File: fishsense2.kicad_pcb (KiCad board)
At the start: 4 copper layers, 97.8 x 109.9 mm, 41 parts, among them J1 Conn_02x10_Odd_Even, J10 USB_B_Micro, J11 Screw_Terminal_01x02, J2 BATT_OUT, J3 BATT_IN, J4 Barrel_Jack_Switch, J5 USB3_A, J6 USB3_A, J7 USB3_A, J8 USB3_A, J9 Barrel_Jack, K1 UMS05-1A80-75L, Q1 Q_NMOS_DGS, Q2 Q_NMOS_DSG, SW1 SW_Reed, SW2 SW_Reed, U5 P783F-Q24-S5-S

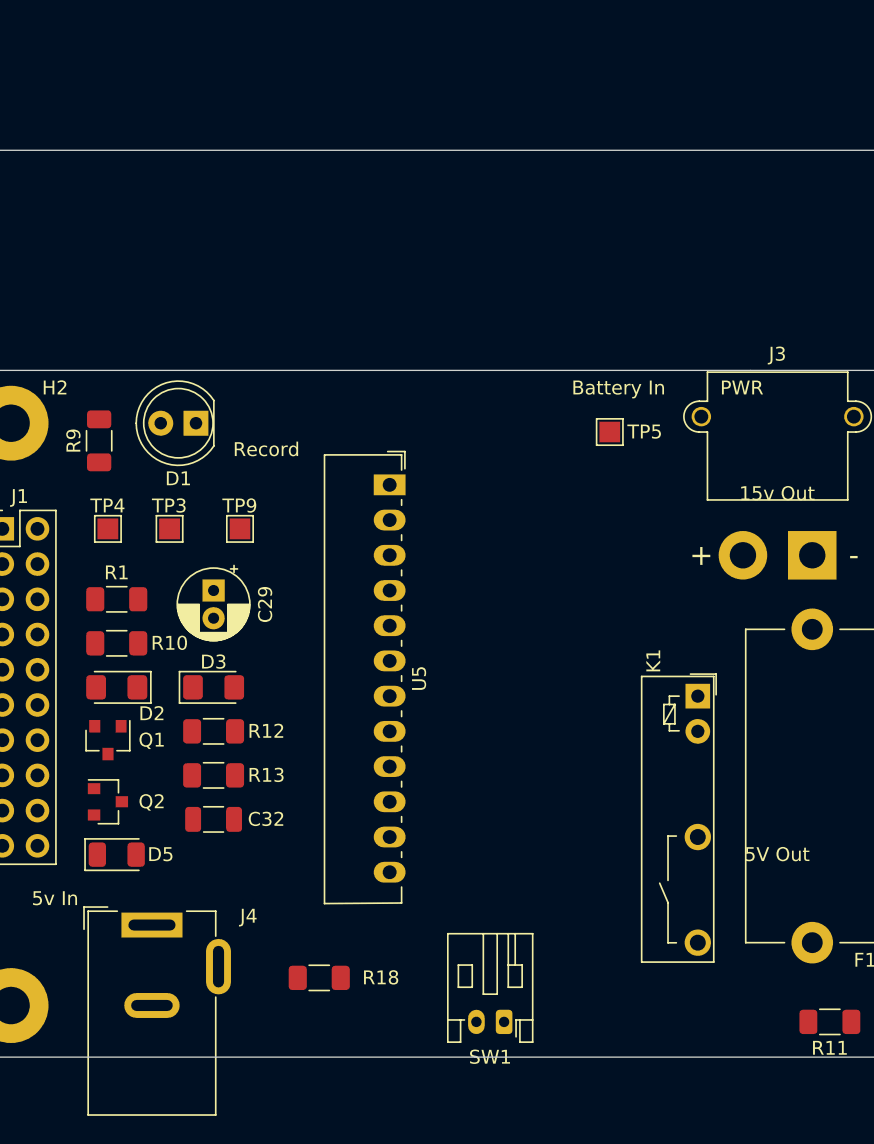
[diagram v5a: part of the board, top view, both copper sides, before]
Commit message: Removed uneeded DC barrel power. Adjusted component values for 12v supply. Checked footprints.
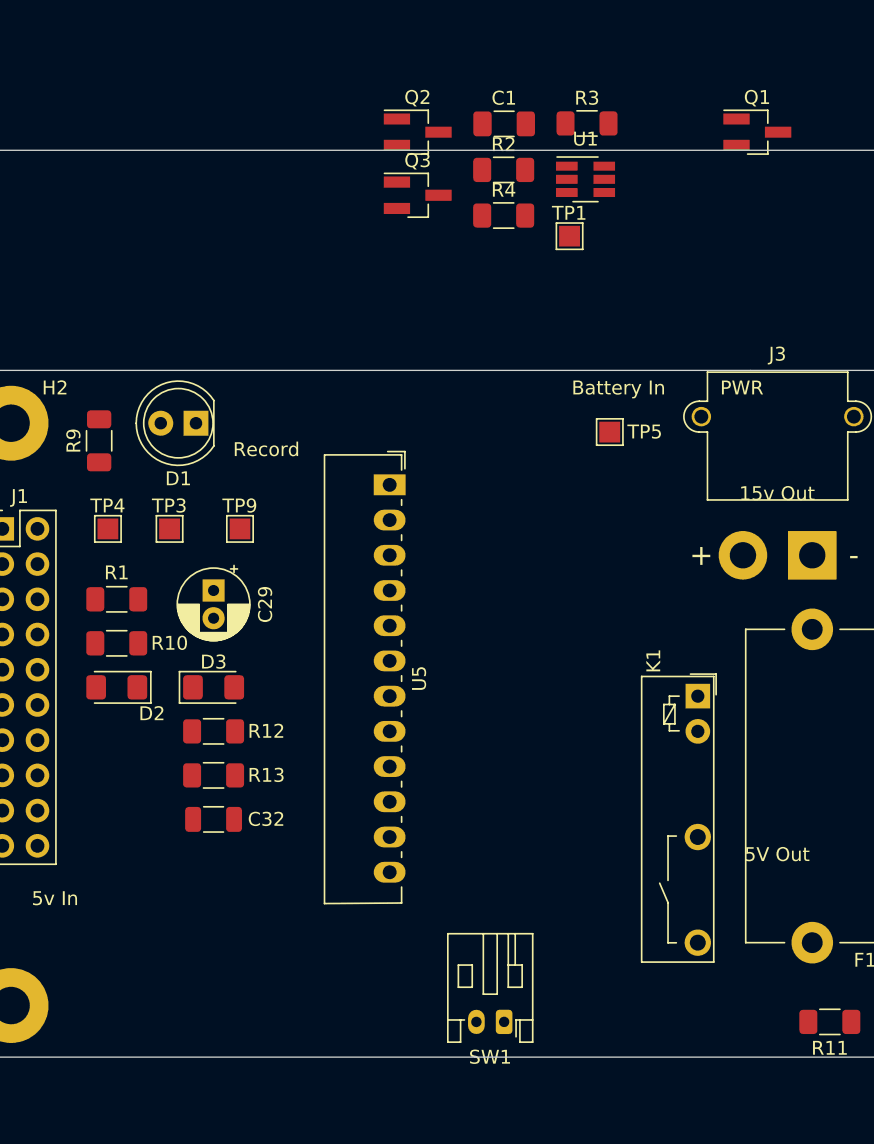
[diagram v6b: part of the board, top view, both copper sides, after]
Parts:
- removed D5: D_Schottky, Diode_SMD:D_1206_3216Metric
- removed J4: Barrel_Jack_Switch, Connector_BarrelJack:BarrelJack_Wuerth_6941xx301002
- removed R18: 125k, Resistor_SMD:R_1206_3216Metric_Pad1.30x1.75mm_HandSolder
- added C1: 10n, Capacitor_SMD:C_1206_3216Metric_Pad1.33x1.80mm_HandSolder, F.Cu at (156.2, 94.0)
- added Q3: Q_NMOS_GSD, Package_TO_SOT_SMD:SOT-23_Handsoldering, F.Cu at (150.0, 99.1)
- added R2: 100k, Resistor_SMD:R_1206_3216Metric_Pad1.30x1.75mm_HandSolder, F.Cu at (156.2, 97.3)
- added R3: 1M69, Resistor_SMD:R_1206_3216Metric_Pad1.30x1.75mm_HandSolder, F.Cu at (162.2, 94.0)
- added R4: 80k, Resistor_SMD:R_1206_3216Metric_Pad1.30x1.75mm_HandSolder, F.Cu at (156.2, 100.6)
- added TP1: Poweroff_OD, TestPoint:TestPoint_Pad_1.5x1.5mm, F.Cu at (160.9, 102.1)
- added U1: TPS3711, Package_TO_SOT_SMD:SOT-23-6_Handsoldering, F.Cu at (162.1, 98.0)
- Q1: value Q_NMOS_DGS -> Q_NMOS_GSD; footprint Package_TO_SOT_SMD:SOT-23 -> Package_TO_SOT_SMD:SOT-23_Handsoldering
- Q2: value Q_NMOS_DSG -> Q_NMOS_GSD; footprint Package_TO_SOT_SMD:SOT-23 -> Package_TO_SOT_SMD:SOT-23_Handsoldering
- R1: value 39k -> 30k
- R11: value 5k6 -> 300
- R12: value 20k -> 100k
- R13: value 40k -> 200k
- moved Q1 64.2 mm to (174.5, 94.6), turned to 0 degrees
- moved Q2 53.2 mm to (150.0, 94.6)
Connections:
- C32 pad 1: Net-(C32-Pad1) -> +5V
- F1 pad 1: +15V -> +12V
- J1 pad 8: REED -> Net-(J1-Pad8)
- J1 pad 9: Net-(J1-Pad9) -> REED
- K1 pad 4: +15V -> +12V
- Q1 pad 1: Net-(D1-Pad1) -> Net-(J1-Pad7)
- Q1 pad 2: Net-(J1-Pad7) -> GND
- Q1 pad 3: GND -> Net-(D1-Pad1)
- Q2 pad 1: /Power/RELAY- -> RELAY_CTL
- Q2 pad 2: /Power/BARREL_OPEN -> Net-(Q2-Pad2)
- Q2 pad 3: RELAY_CTL -> /Power/RELAY-
- R11 pad 1: +15V -> +12V
- R12 pad 1: +5V -> +12V
- SW1 pad 2: Net-(J1-Pad9) -> Net-(J1-Pad8)
- U5 pad 10: Net-(C32-Pad1) -> +5V
- U5 pad 11: Net-(C32-Pad1) -> +5V
- U5 pad 9: Net-(C32-Pad1) -> +5V

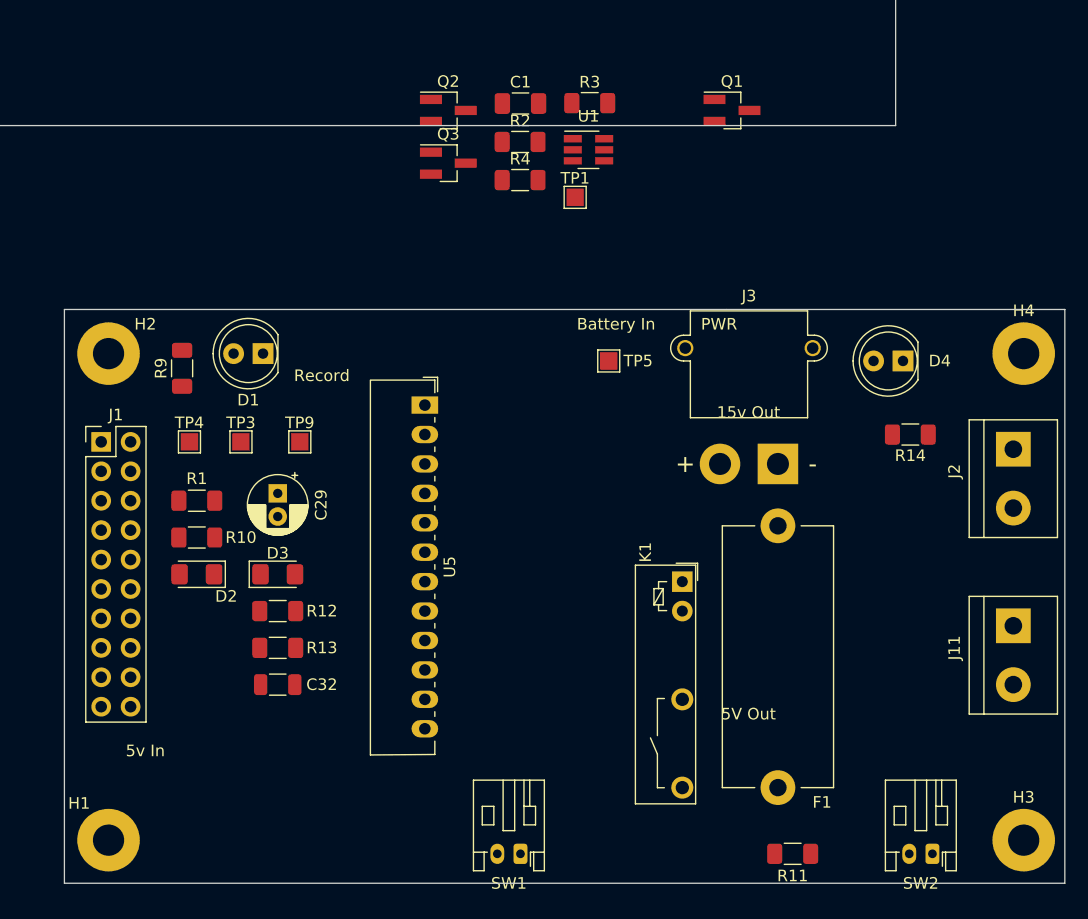
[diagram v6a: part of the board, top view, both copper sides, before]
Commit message: Moved components around on PCB. Fixed fuse footprint.
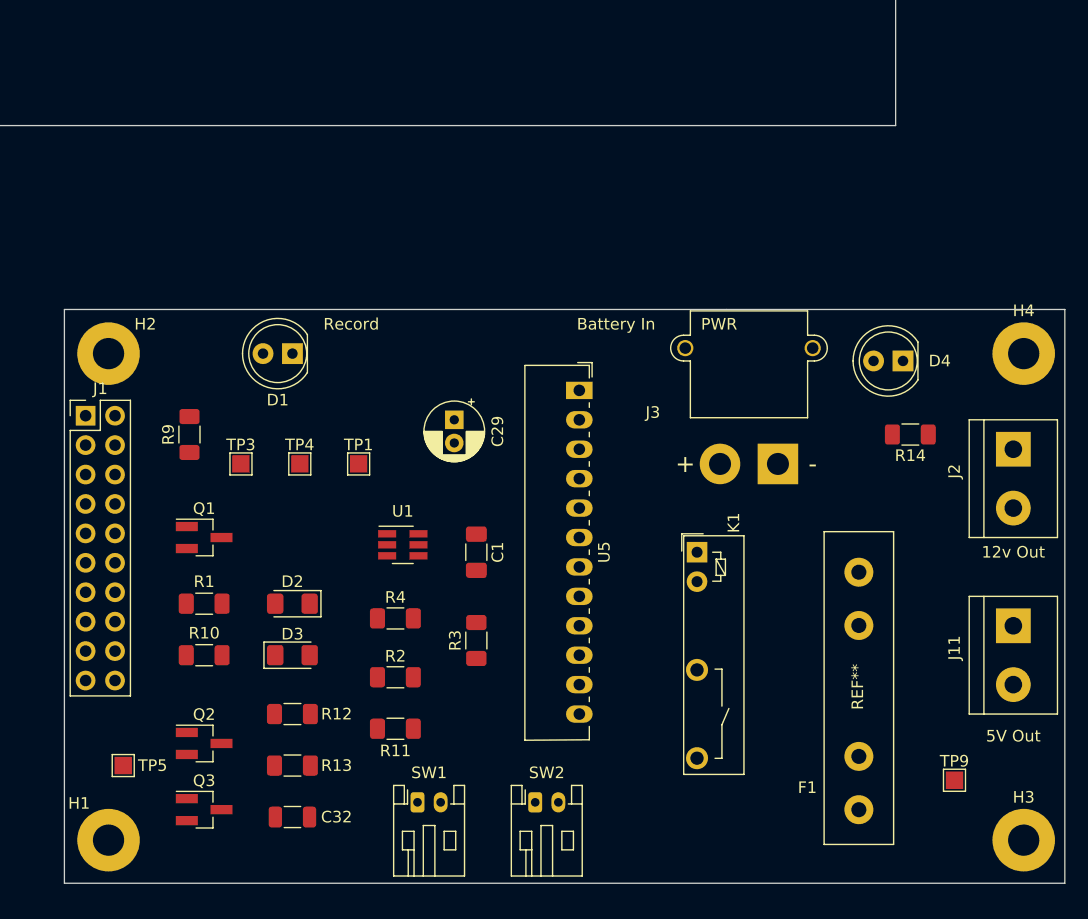
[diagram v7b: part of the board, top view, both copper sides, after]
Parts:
- F1: footprint Fuse:Fuseholder_Cylinder-5x20mm_Stelvio-Kontek_PTF78_Horizontal_Open -> fishsense2:5mm_Fuse_Clips
- moved TP9 63.6 mm to (193.7, 152.4)
- moved Q3 59.7 mm to (128.9, 154.9)
- moved Q1 58.6 mm to (128.9, 131.4)
- moved Q2 58.6 mm to (128.9, 149.2)
- moved TP5 54.6 mm to (121.9, 151.1)
- moved R2 47.4 mm to (145.4, 143.5)
- moved R3 47.4 mm to (152.4, 140.3), turned to 90 degrees
- moved R4 39.3 mm to (145.4, 138.4)
- moved C1 38.9 mm to (152.4, 132.7), turned to 270 degrees
- moved U1 37.7 mm to (146.1, 132.1)
- moved R11 35.9 mm to (145.4, 148.0)
- moved SW2 34.6 mm to (157.5, 154.3), turned to 0 degrees
- moved TP1 29.6 mm to (142.2, 125.1)
- moved C29 16.5 mm to (150.5, 121.3)
- moved U5 13.4 mm to (161.3, 118.7)
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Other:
- board text added: "12v Out"
- board text removed: "15v Out"
- board text removed: "5v In"

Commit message: Routed traces.
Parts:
- removed J10: USB_B_Micro, Connector_USB:USB_Micro-B_GCT_USB3076-30-A
- removed J5, J6, J7, J8: USB3_A, Connector_USB:USB3_A_Molex_48393-001
- removed J9: Barrel_Jack, Connector_BarrelJack:BarrelJack_Horizontal
- F1: footprint fishsense2:5mm_Fuse_Clips -> Fuse:Fuseholder_Cylinder-5x20mm_Stelvio-Kontek_PTF78_Horizontal_Open
- moved C32 30.9 mm to (165.7, 145.4), turned to 90 degrees
- turned R2 to 180 degrees
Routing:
- net +12V: track 0.00 -> 75.8 mm, vias 0 -> 2
- net /Power/RELAY+: track 0.00 -> 67.2 mm, vias 0 -> 1
- net /Power/BATT_SWITCHED: track 0.00 -> 65.0 mm
- net +5V: track 0.00 -> 64.7 mm, vias 0 -> 4
- net /Power/RELAY-: track 0.00 -> 62.1 mm, vias 0 -> 1
- net Net-(J1-Pad8): track 0.00 -> 61.9 mm, vias 0 -> 1
- net /Power/POWEROFF_OD: track 0.00 -> 47.0 mm, vias 0 -> 3
- net RELAY_CTL: track 0.00 -> 45.1 mm, vias 0 -> 2
- net Net-(D2-Pad2): track 0.00 -> 34.7 mm
- net Net-(D1-Pad1): track 0.00 -> 18.4 mm
- net Net-(F1-Pad2): track 0.00 -> 16.9 mm
- net REED: track 0.00 -> 16.6 mm
- net Net-(R11-Pad2): track 0.00 -> 16.4 mm
- net Net-(R3-Pad2): track 0.00 -> 15.2 mm
- net Net-(J1-Pad7): track 0.00 -> 10.7 mm
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- added copper zone on B.Cu, net +5V
- added copper zone on F.Cu, net /Power/BATT_SWITCHED
- added copper zone on B.Cu, net GND
- added copper zone on F.Cu, net GND
- removed copper zone on In1.Cu, net GND
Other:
- board size 97.8 x 109.9 mm -> 86.4 x 49.5 mm
- copper layers 4 -> 2
- net class Default: clearance 0.127 -> 0.2; trace_width 0.2 -> 0.5
- net class USB removed
- rule trace_clearance: 0.127 -> 0.2
